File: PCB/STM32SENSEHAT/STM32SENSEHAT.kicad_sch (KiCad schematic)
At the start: 0 parts

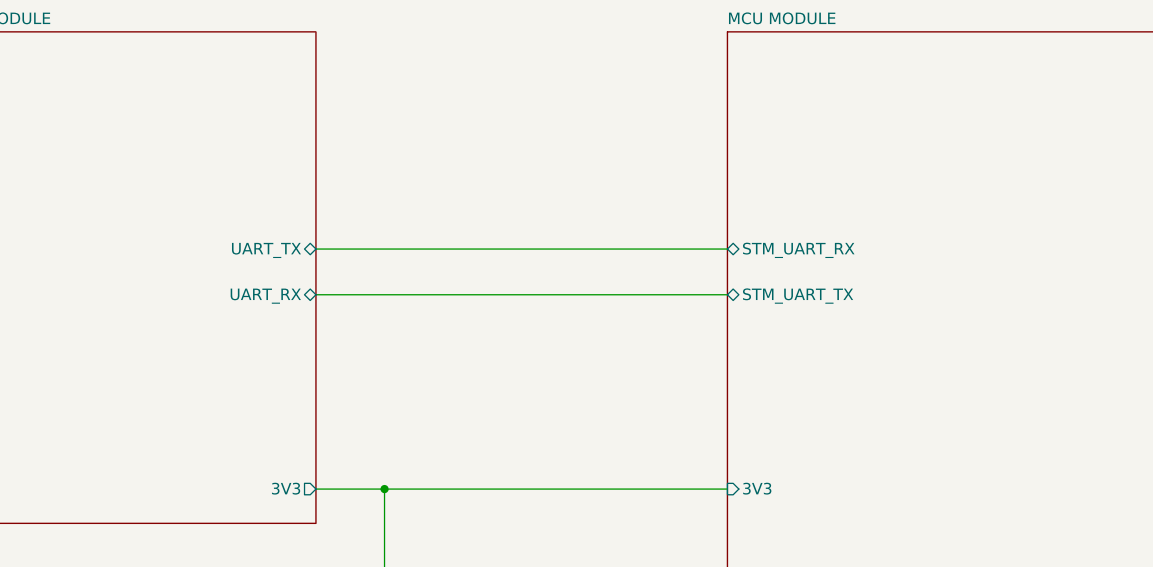
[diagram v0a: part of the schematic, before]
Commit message: Removed the extra sensor, Modified BME280 interfacing and FTDI UART pins. Added Manual Reset to MCU and configured BOOT pin
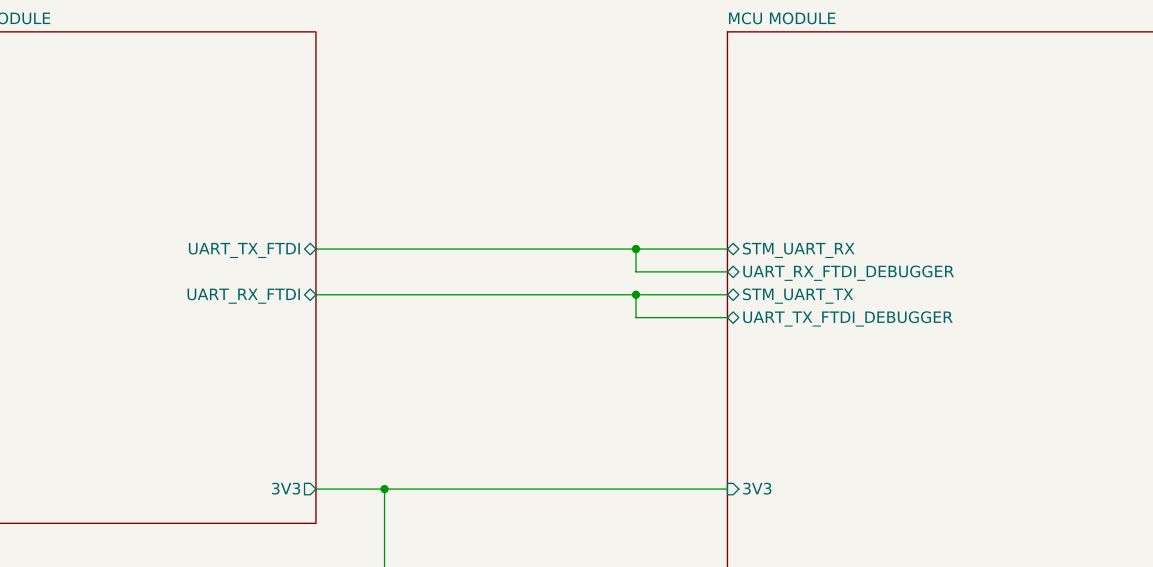
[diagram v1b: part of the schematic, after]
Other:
- sheet MCU MODULE ports: added UART_RX_FTDI_DEBUGGER, UART_TX_FTDI_DEBUGGER; removed none
- sheet POWER MANAGEMENT MODULE ports: added UART_RX_FTDI, UART_TX_FTDI; removed UART_RX, UART_TX

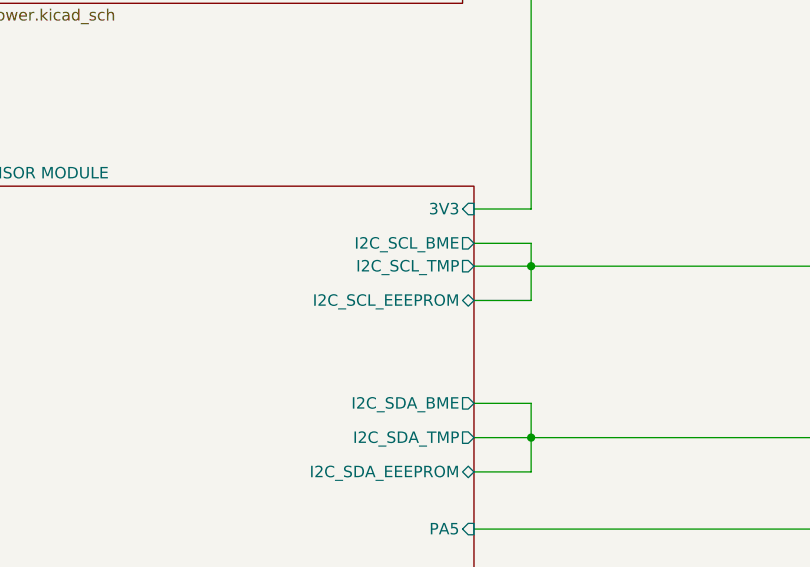
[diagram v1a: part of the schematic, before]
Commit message: Add STM32SENSEHAT, power, sensor, and mcu schematic file
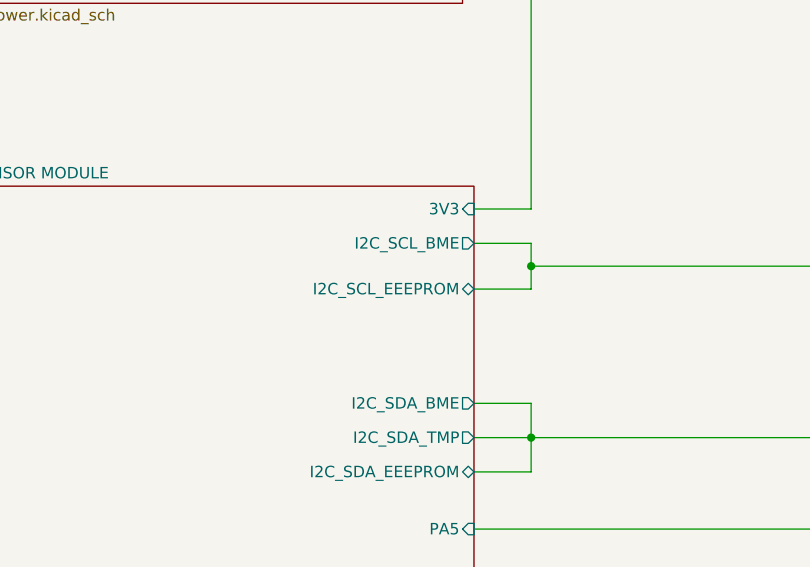
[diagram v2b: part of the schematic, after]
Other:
- sheet SENSOR MODULE ports: added none; removed I2C_SCL_TMP
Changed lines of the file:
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@@
-    (stroke (width 0) (type default))
-  )
-  (wire (pts (xy 92.71 106.68) (xy 99.06 106.68))
     (stroke (width 0) (type default))
   )
@@
     (stroke (width 0) (type default))
   )
-  (wire (pts (xy 99.06 106.68) (xy 99.06 110.49))
+  (wire (pts (xy 99.06 106.68) (xy 99.06 109.22))
     (stroke (width 0) (type default))
   )
@@
     (stroke (width 0) (type default))
   )
-  (wire (pts (xy 92.71 110.49) (xy 99.06 110.49))
+  (wire (pts (xy 92.71 109.22) (xy 99.06 109.22))
     (stroke (width 0) (type default))
   )
@@
       (effects (font (size 1.27 1.27)) (justify right))
     )
-    (pin "I2C_SCL_TMP" output (at 92.71 106.68 0)
+    (pin "I2C_SCL_EEEPROM" bidirectional (at 92.71 109.22 0)
       (effects (font (size 1.27 1.27)) (justify right))
     )
-    (pin "I2C_SCL_EEEPROM" bidirectional (at 92.71 110.49 0)
-      (effects (font (size 1.27 1.27)) (justify right))
-    )

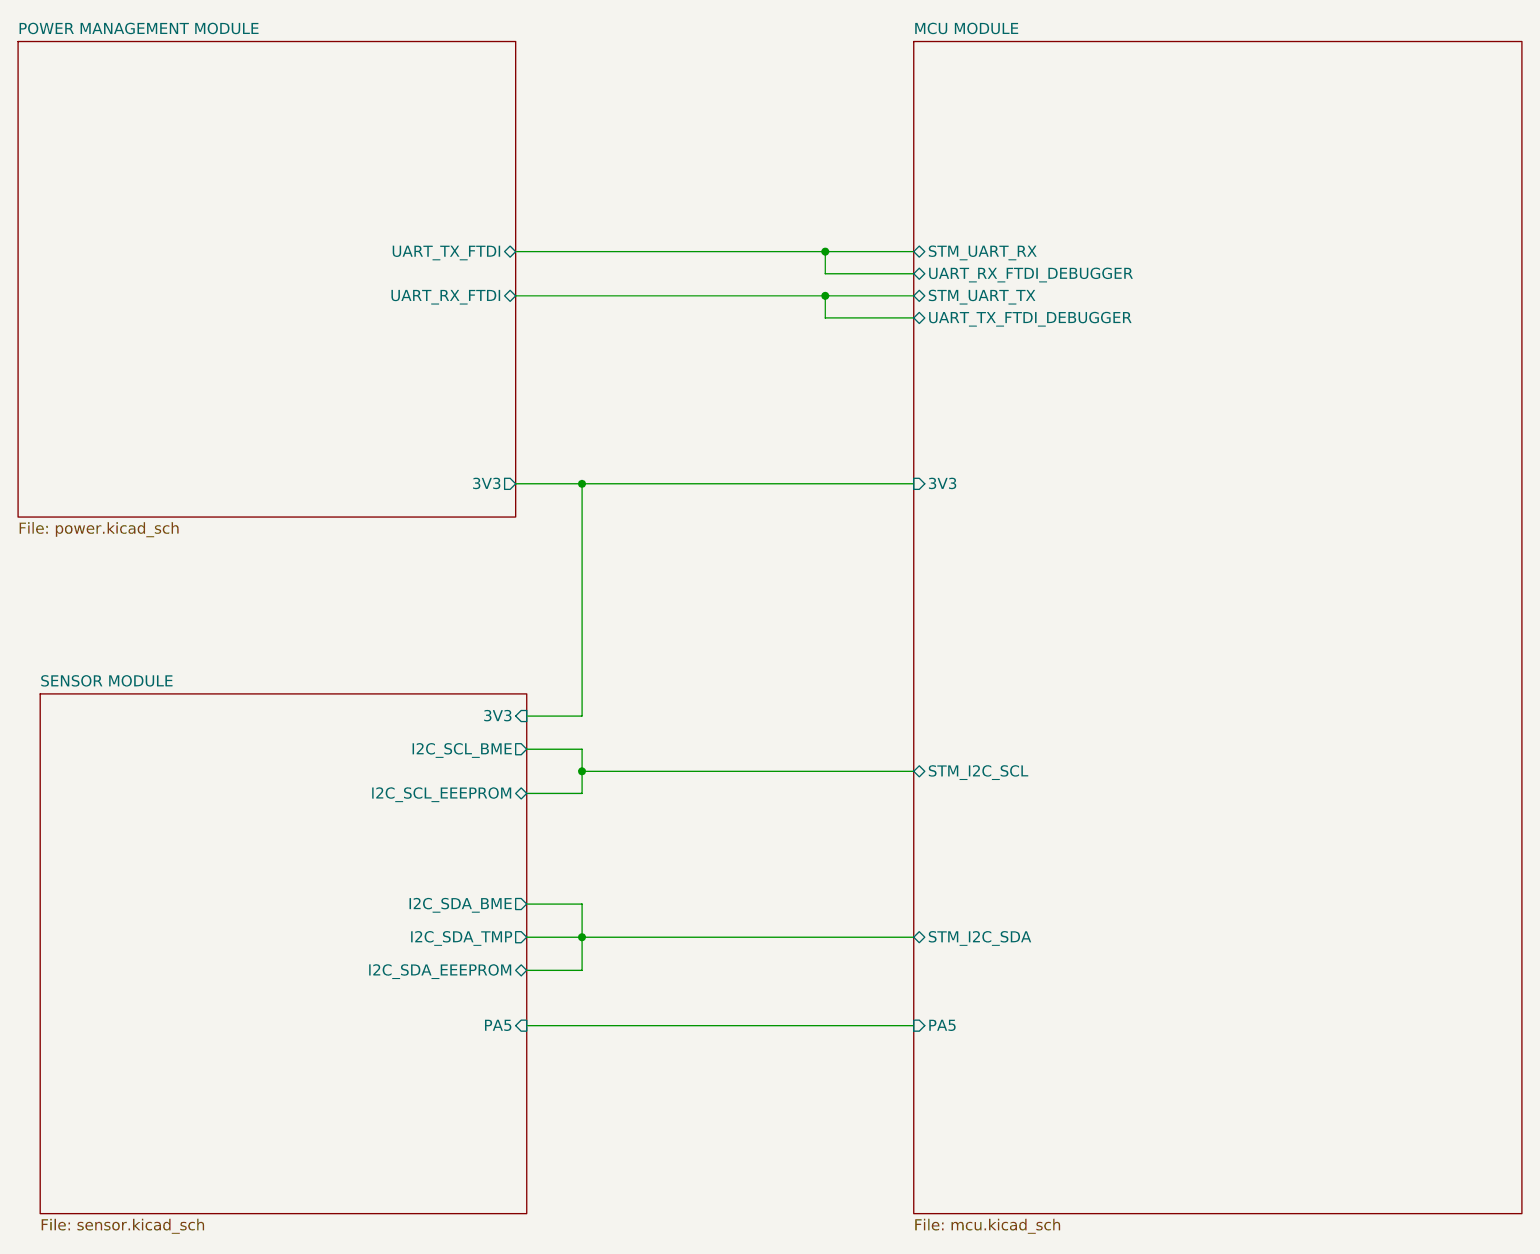
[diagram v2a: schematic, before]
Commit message: Revised schematics. Moved USB and EEPROM sub modules to MCU sheet and and rectified the top sheet accordingly
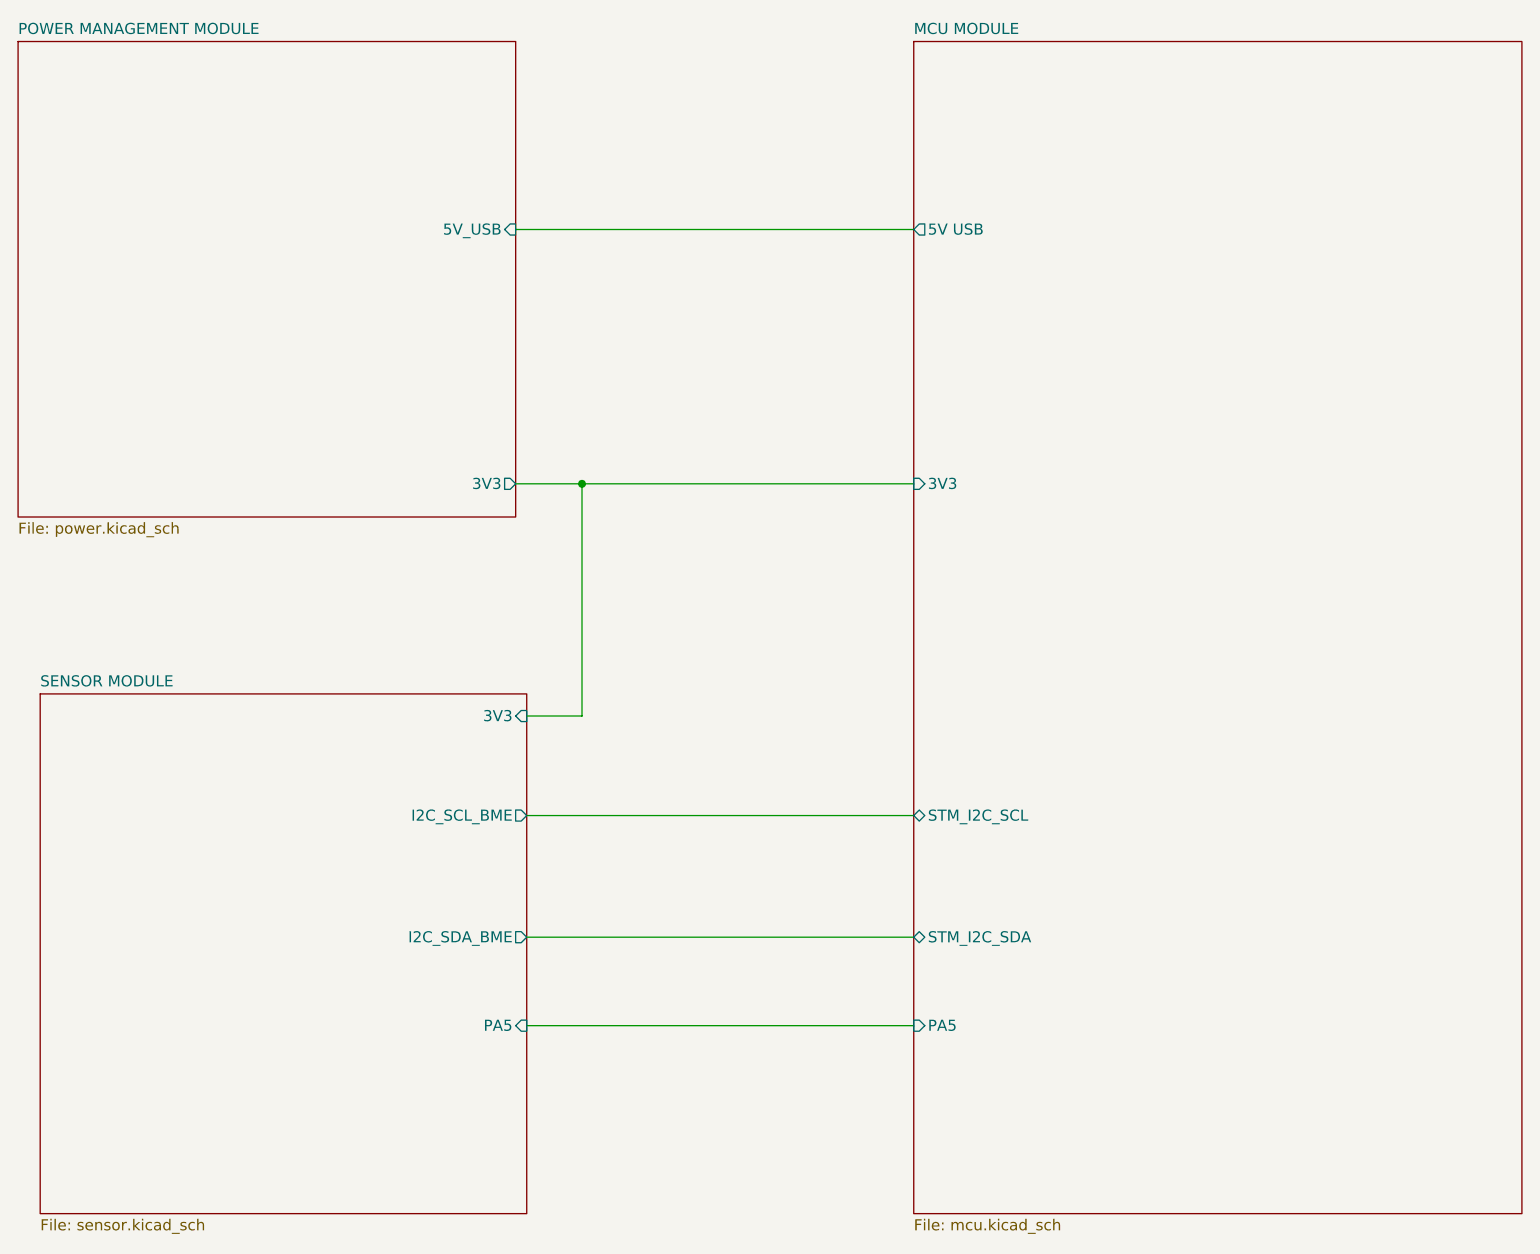
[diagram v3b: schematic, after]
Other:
- sheet MCU MODULE ports: added 5V USB; removed STM_UART_RX, STM_UART_TX, UART_RX_FTDI_DEBUGGER, UART_TX_FTDI_DEBUGGER
- sheet POWER MANAGEMENT MODULE ports: added 5V_USB; removed UART_RX_FTDI, UART_TX_FTDI
- sheet SENSOR MODULE ports: added none; removed I2C_SCL_EEEPROM, I2C_SDA_EEEPROM, I2C_SDA_TMP
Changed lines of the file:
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@@
   (junction (at 99.06 73.66) (diameter 0) (color 0 0 0 0)
-  )
-  (junction (at 127 52.07) (diameter 0) (color 0 0 0 0)
-  )
-  (junction (at 99.06 125.73) (diameter 0) (color 0 0 0 0)
-  )
-  (junction (at 99.06 106.68) (diameter 0) (color 0 0 0 0)
-  )
-  (junction (at 127 46.99) (diameter 0) (color 0 0 0 0)
-  )
-  (wire (pts (xy 127 52.07) (xy 137.16 52.07))
-    (stroke (width 0) (type default))
-  )
-  (wire (pts (xy 91.44 46.99) (xy 127 46.99))
-    (stroke (width 0) (type default))
-  )
-  (wire (pts (xy 99.06 106.68) (xy 137.16 106.68))
-    (stroke (width 0) (type default))
   )
   (wire (pts (xy 91.44 73.66) (xy 99.06 73.66))
@@
     (stroke (width 0) (type default))
   )
-  (wire (pts (xy 99.06 121.92) (xy 99.06 125.73))
+  (wire (pts (xy 91.44 44.45) (xy 137.16 44.45))
     (stroke (width 0) (type default))
   )
-  (wire (pts (xy 92.71 121.92) (xy 99.06 121.92))
-    (stroke (width 0) (type default))
-  )
-  (wire (pts (xy 92.71 125.73) (xy 99.06 125.73))
-    (stroke (width 0) (type default))
-  )
-  (wire (pts (xy 91.44 52.07) (xy 127 52.07))
-    (stroke (width 0) (type default))
-  )
-  (wire (pts (xy 99.06 106.68) (xy 99.06 109.22))
+  (wire (pts (xy 92.71 125.73) (xy 137.16 125.73))
     (stroke (width 0) (type default))
   )
@@
     (stroke (width 0) (type default))
   )
-  (wire (pts (xy 137.16 49.53) (xy 127 49.53))
-    (stroke (width 0) (type default))
-  )
   (wire (pts (xy 99.06 100.33) (xy 99.06 73.66))
     (stroke (width 0) (type default))
   )
-  (wire (pts (xy 127 54.61) (xy 127 52.07))
+  (wire (pts (xy 92.71 111.76) (xy 137.16 111.76))
     (stroke (width 0) (type default))
   )
-  (wire (pts (xy 127 46.99) (xy 137.16 46.99))
-    (stroke (width 0) (type default))
-  )
-  (wire (pts (xy 99.06 125.73) (xy 99.06 129.54))
-    (stroke (width 0) (type default))
-  )
-  (wire (pts (xy 127 49.53) (xy 127 46.99))
-    (stroke (width 0) (type default))
-  )
-  (wire (pts (xy 99.06 129.54) (xy 92.71 129.54))
-    (stroke (width 0) (type default))
-  )
   (wire (pts (xy 92.71 135.89) (xy 137.16 135.89))
-    (stroke (width 0) (type default))
-  )
-  (wire (pts (xy 92.71 104.14) (xy 99.06 104.14))
-    (stroke (width 0) (type default))
-  )
-  (wire (pts (xy 92.71 109.22) (xy 99.06 109.22))
-    (stroke (width 0) (type default))
-  )
-  (wire (pts (xy 137.16 54.61) (xy 127 54.61))
-    (stroke (width 0) (type default))
-  )
-  (wire (pts (xy 99.06 104.14) (xy 99.06 106.68))
-    (stroke (width 0) (type default))
-  )
-  (wire (pts (xy 99.06 125.73) (xy 137.16 125.73))
     (stroke (width 0) (type default))
   )
@@
       (effects (font (size 1.27 1.27)) (justify right))
     )
-    (pin "I2C_SDA_BME" output (at 92.71 121.92 0)
+    (pin "I2C_SDA_BME" output (at 92.71 125.73 0)
       (effects (font (size 1.27 1.27)) (justify right))
     )
-    (pin "I2C_SCL_BME" output (at 92.71 104.14 0)
+    (pin "3V3" input (at 92.71 100.33 0)
       (effects (font (size 1.27 1.27)) (justify right))
     )
-    (pin "I2C_SCL_EEEPROM" bidirectional (at 92.71 109.22 0)
-      (effects (font (size 1.27 1.27)) (justify right))
-    )
-    (pin "I2C_SDA_TMP" output (at 92.71 125.73 0)
-      (effects (font (size 1.27 1.27)) (justify right))
-    )
-    (pin "I2C_SDA_EEEPROM" bidirectional (at 92.71 129.54 0)
-      (effects (font (size 1.27 1.27)) (justify right))
-    )
-    (pin "3V3" input (at 92.71 100.33 0)
+    (pin "I2C_SCL_BME" output (at 92.71 111.76 0)
       (effects (font (size 1.27 1.27)) (justify right))
     )
@@
       (effects (font (size 1.27 1.27)) (justify left top))
     )
-    (pin "STM_UART_RX" bidirectional (at 137.16 46.99 180)
-      (effects (font (size 1.27 1.27)) (justify left))
-    )
-    (pin "STM_UART_TX" bidirectional (at 137.16 52.07 180)
-      (effects (font (size 1.27 1.27)) (justify left))
-    )
-    (pin "STM_I2C_SCL" bidirectional (at 137.16 106.68 180)
-      (effects (font (size 1.27 1.27)) (justify left))
-    )
     (pin "STM_I2C_SDA" bidirectional (at 137.16 125.73 180)
       (effects (font (size 1.27 1.27)) (justify left))
@@
       (effects (font (size 1.27 1.27)) (justify left))
     )
-    (pin "UART_TX_FTDI_DEBUGGER" bidirectional (at 137.16 54.61 180)
+    (pin "5V USB" output (at 137.16 44.45 180)
       (effects (font (size 1.27 1.27)) (justify left))
     )
-    (pin "UART_RX_FTDI_DEBUGGER" bidirectional (at 137.16 49.53 180)
+    (pin "STM_I2C_SCL" bidirectional (at 137.16 111.76 180)
       (effects (font (size 1.27 1.27)) (justify left))
     )
@@
       (effects (font (size 1.27 1.27)) (justify right))
     )
-    (pin "UART_TX_FTDI" bidirectional (at 91.44 46.99 0)
+    (pin "5V_USB" input (at 91.44 44.45 0)
       (effects (font (size 1.27 1.27)) (justify right))
     )
-    (pin "UART_RX_FTDI" bidirectional (at 91.44 52.07 0)
-      (effects (font (size 1.27 1.27)) (justify right))
-    )
